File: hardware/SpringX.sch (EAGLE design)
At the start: 12 parts, among them U1 MCP1703-5002E/CB, U2 MCP602ST, X1 87438-03

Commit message: minor tweaks to labels placement / size, board dimension and schematics
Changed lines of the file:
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@@
 <?xml version="1.0" encoding="utf-8"?>
 <!DOCTYPE eagle SYSTEM "eagle.dtd">
-<eagle version="6.4">
+<eagle version="6.5.0">
 <drawing>
 <settings>
@@
 <grid distance="0.1" unitdist="inch" unit="inch" style="lines" multiple="1" display="no" altdistance="0.01" altunitdist="inch" altunit="inch"/>
 <layers>
-<layer number="1" name="Top" color="4" fill="1" visible="yes" active="no"/>
-<layer number="16" name="Bottom" color="1" fill="1" visible="yes" active="no"/>
-<layer number="17" name="Pads" color="2" fill="1" visible="yes" active="no"/>
-<layer number="18" name="Vias" color="2" fill="1" visible="yes" active="no"/>
-<layer number="19" name="Unrouted" color="6" fill="1" visible="yes" active="no"/>
-<layer number="20" name="Dimension" color="15" fill="1" visible="yes" active="no"/>
-<layer number="21" name="tPlace" color="7" fill="1" visible="yes" active="no"/>
-<layer number="22" name="bPlace" color="7" fill="1" visible="yes" active="no"/>
-<layer number="23" name="tOrigins" color="15" fill="1" visible="yes" active="no"/>
-<layer number="24" name="bOrigins" color="15" fill="1" visible="yes" active="no"/>
-<layer number="25" name="tNames" color="7" fill="1" visible="yes" active="no"/>
-<layer number="26" name="bNames" color="7" fill="1" visible="yes" active="no"/>
-<layer number="27" name="tValues" color="7" fill="1" visible="yes" active="no"/>
-<layer number="28" name="bValues" color="7" fill="1" visible="yes" active="no"/>
+<layer number="1" name="Top" color="4" fill="1" visible="no" active="no"/>
+<layer number="16" name="Bottom" color="1" fill="1" visible="no" active="no"/>
+<layer number="17" name="Pads" color="2" fill="1" visible="no" active="no"/>
+<layer number="18" name="Vias" color="2" fill="1" visible="no" active="no"/>
+<layer number="19" name="Unrouted" color="6" fill="1" visible="no" active="no"/>
+<layer number="20" name="Dimension" color="15" fill="1" visible="no" active="no"/>
+<layer number="21" name="tPlace" color="7" fill="1" visible="no" active="no"/>
+<layer number="22" name="bPlace" color="7" fill="1" visible="no" active="no"/>
+<layer number="23" name="tOrigins" color="15" fill="1" visible="no" active="no"/>
+<layer number="24" name="bOrigins" color="15" fill="1" visible="no" active="no"/>
+<layer number="25" name="tNames" color="7" fill="1" visible="no" active="no"/>
+<layer number="26" name="bNames" color="7" fill="1" visible="no" active="no"/>
+<layer number="27" name="tValues" color="7" fill="1" visible="no" active="no"/>
+<layer number="28" name="bValues" color="7" fill="1" visible="no" active="no"/>
 <layer number="29" name="tStop" color="7" fill="3" visible="no" active="no"/>
 <layer number="30" name="bStop" color="7" fill="6" visible="no" active="no"/>
@@
 <layer number="35" name="tGlue" color="7" fill="4" visible="no" active="no"/>
 <layer number="36" name="bGlue" color="7" fill="5" visible="no" active="no"/>
-<layer number="37" name="tTest" color="7" fill="1" visible="yes" active="no"/>
-<layer number="38" name="bTest" color="7" fill="1" visible="yes" active="no"/>
+<layer number="37" name="tTest" color="7" fill="1" visible="no" active="no"/>
+<layer number="38" name="bTest" color="7" fill="1" visible="no" active="no"/>
 <layer number="39" name="tKeepout" color="4" fill="11" visible="no" active="no"/>
 <layer number="40" name="bKeepout" color="1" fill="11" visible="no" active="no"/>
@@
 <layer number="44" name="Drills" color="7" fill="1" visible="no" active="no"/>
 <layer number="45" name="Holes" color="7" fill="1" visible="no" active="no"/>
-<layer number="46" name="Milling" color="3" fill="1" visible="yes" active="no"/>
-<layer number="47" name="Measures" color="7" fill="1" visible="yes" active="no"/>
-<layer number="48" name="Document" color="7" fill="1" visible="yes" active="no"/>
-<layer number="49" name="Reference" color="7" fill="1" visible="yes" active="no"/>
-<layer number="50" name="dxf" color="7" fill="1" visible="yes" active="no"/>
-<layer number="51" name="tDocu" color="7" fill="1" visible="yes" active="no"/>
-<layer number="52" name="bDocu" color="7" fill="1" visible="yes" active="no"/>
+<layer number="46" name="Milling" color="3" fill="1" visible="no" active="no"/>
+<layer number="47" name="Measures" color="7" fill="1" visible="no" active="no"/>
+<layer number="48" name="Document" color="7" fill="1" visible="no" active="no"/>
+<layer number="49" name="Reference" color="7" fill="1" visible="no" active="no"/>
+<layer number="50" name="dxf" color="7" fill="1" visible="no" active="no"/>
+<layer number="51" name="tDocu" color="7" fill="1" visible="no" active="no"/>
+<layer number="52" name="bDocu" color="7" fill="1" visible="no" active="no"/>
 <layer number="91" name="Nets" color="2" fill="1" visible="yes" active="yes"/>
 <layer number="92" name="Busses" color="1" fill="1" visible="yes" active="yes"/>
@@
 <pinref part="U2" gate="A" pin="-IN"/>
 <wire x1="109.22" y1="15.24" x2="111.76" y2="15.24" width="0.1524" layer="91"/>
+<junction x="109.22" y="15.24"/>
 </segment>
 </net>
@@
 <pinref part="U2" gate="B" pin="-IN"/>
 <wire x1="63.5" y1="12.7" x2="66.04" y2="12.7" width="0.1524" layer="91"/>
+<junction x="91.44" y="15.24"/>
 </segment>
 </net>
@@
 <wire x1="127" y1="17.78" x2="137.16" y2="17.78" width="0.1524" layer="91"/>
 <label x="144.78" y="17.78" size="1.778" layer="95" xref="yes"/>
-</segment>
-<segment>
+<junction x="137.16" y="17.78"/>
+</segment>
+<segment>

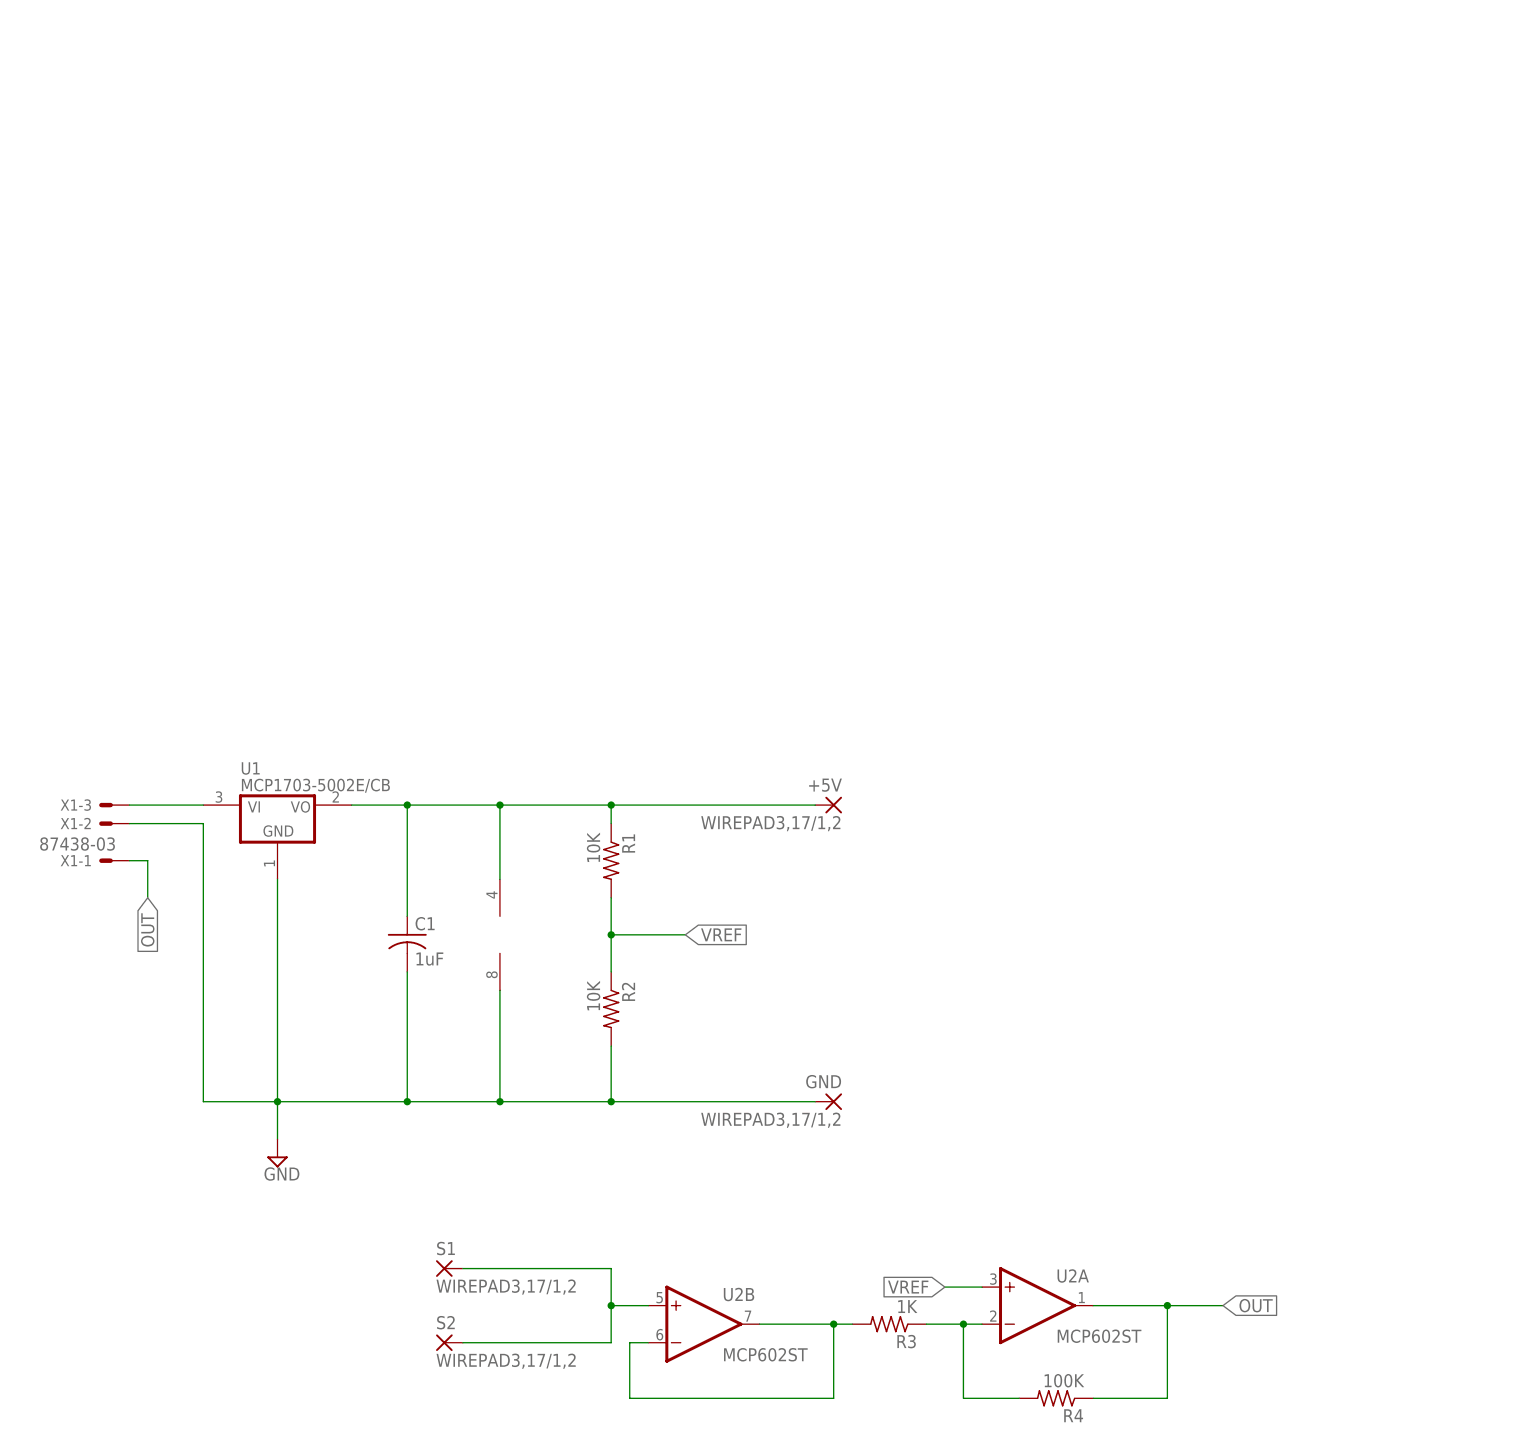
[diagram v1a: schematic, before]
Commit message: Major revision to board. Corrected error - Op amp power and ground pins reversed Changed to Molex KK connector type. Complete board re-layout.
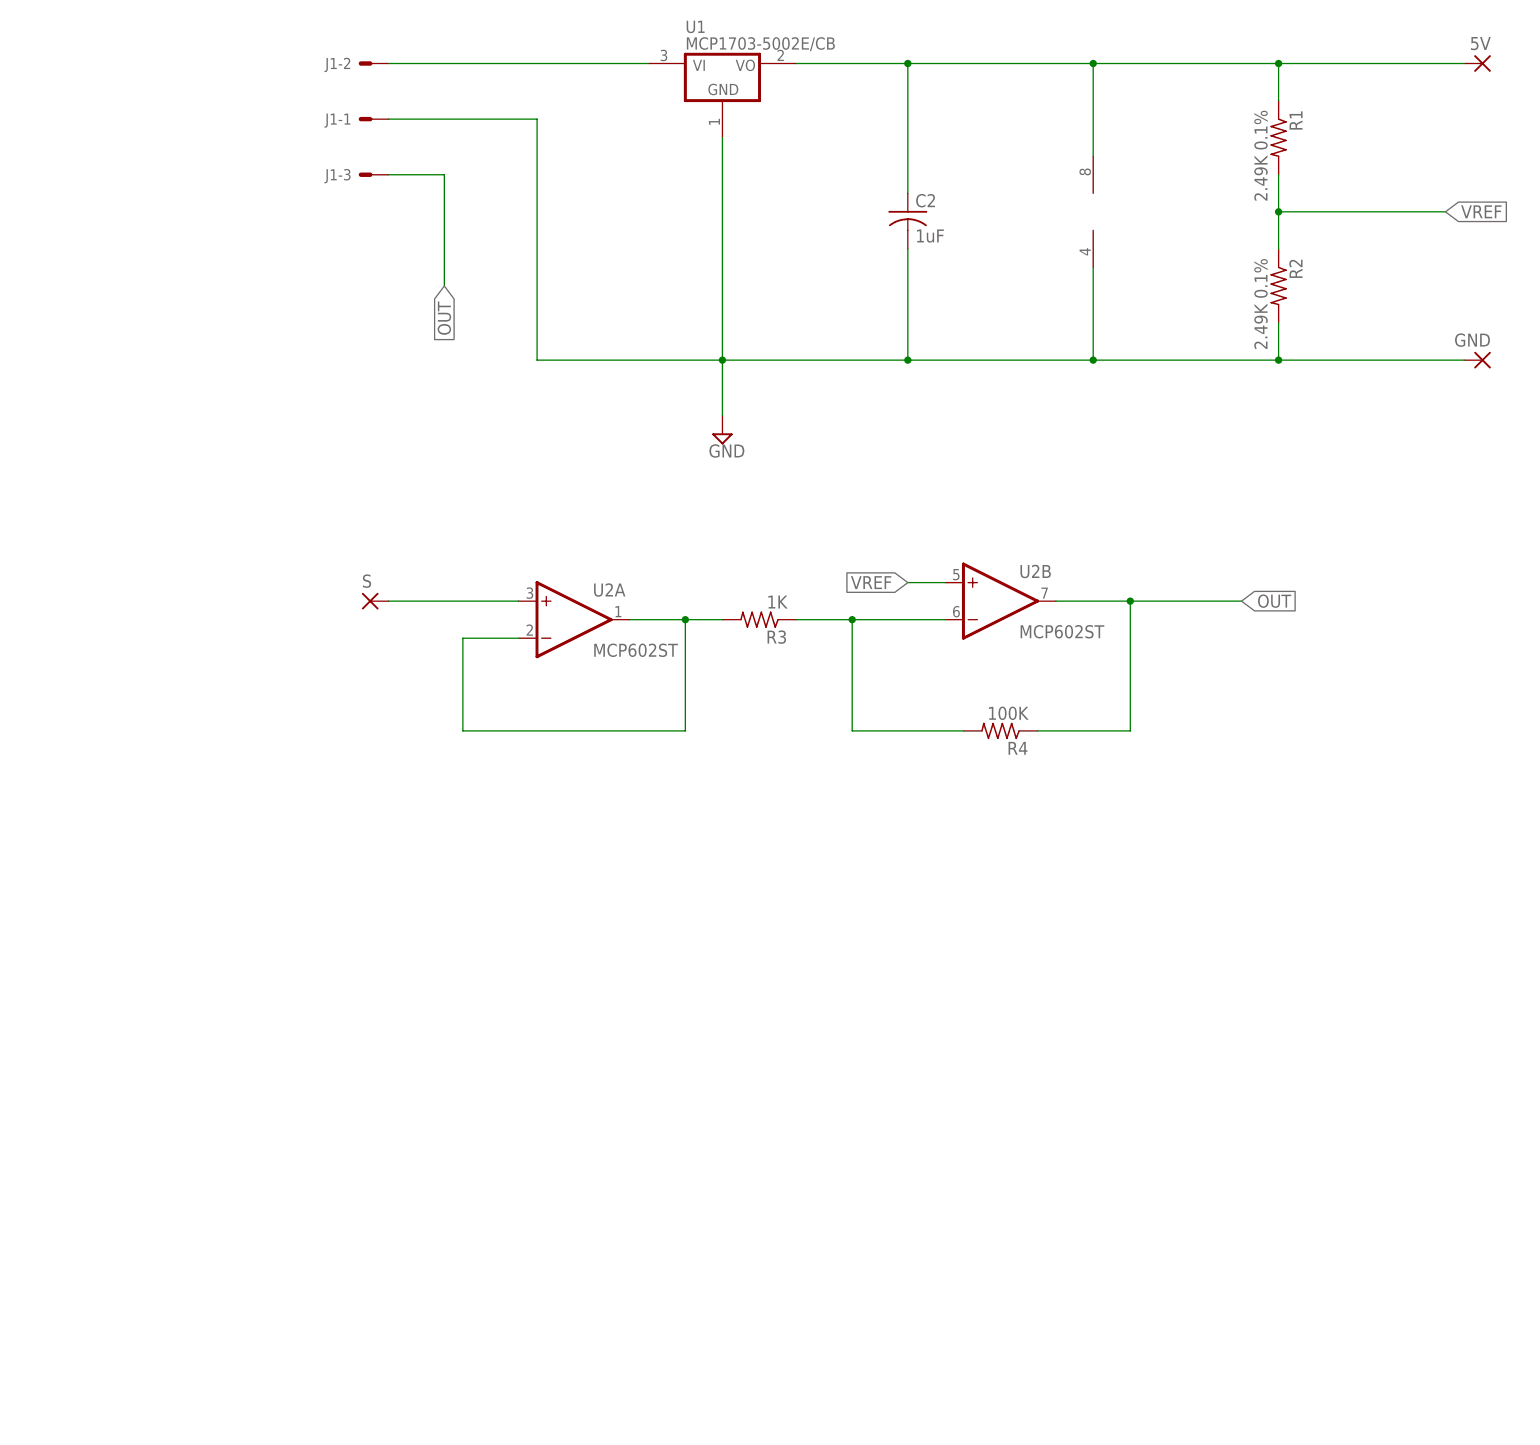
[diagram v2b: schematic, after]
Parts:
- removed +5V, S1, S2: WIREPAD3,17/1,2, wirepad:WIREPAD3,17/1,2
- removed C1: 1uF, rcl:C-USC0603
- removed X1: 87438-03, con-molex:87438-03
- added 5V, S: (no value), wirepad:2,15/1,0
- added C2: 1uF, rcl:C-USC0603
- added J1: (no value), ep_molex_6410_7395-02:22-05-7038-03
- GND: value WIREPAD3,17/1,2 -> (none); device wirepad:WIREPAD3,17/1,2 -> wirepad:2,15/1,0
- R1, R2: value 10K -> 2.49K 0.1%
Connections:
- removed net N$1: U1.VI, X1-3.S
- removed net STR: S1.P, S2.P, U2B.+IN
- new net N$3: S.P, U2A.+IN
- new net VI: J1-2.S, U1.VI
- net 5V: now also 5V.P, C2.1, U2P.V+; no longer +5V.P, C1.1, U2P.V-
- net GND: now also C2.2, J1-1.S, U2P.V-; no longer C1.2, U2P.V+, X1-2.S
- net N$2: now also U2A.-IN, U2A.OUT; no longer U2B.-IN, U2B.OUT
- net N$4: now also U2B.-IN; no longer U2A.-IN
- net OUT: now also J1-3.S, U2B.OUT; no longer U2A.OUT, X1-1.S
- net VREF: now also U2B.+IN; no longer U2A.+IN
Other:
- moved on the sheet: R1, R2, R3, R4, U1, U2A, U2B
